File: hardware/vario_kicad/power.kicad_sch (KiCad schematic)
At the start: 25 parts, among them Q1 NMOS, Q2 PMOS, U4 USB C connector

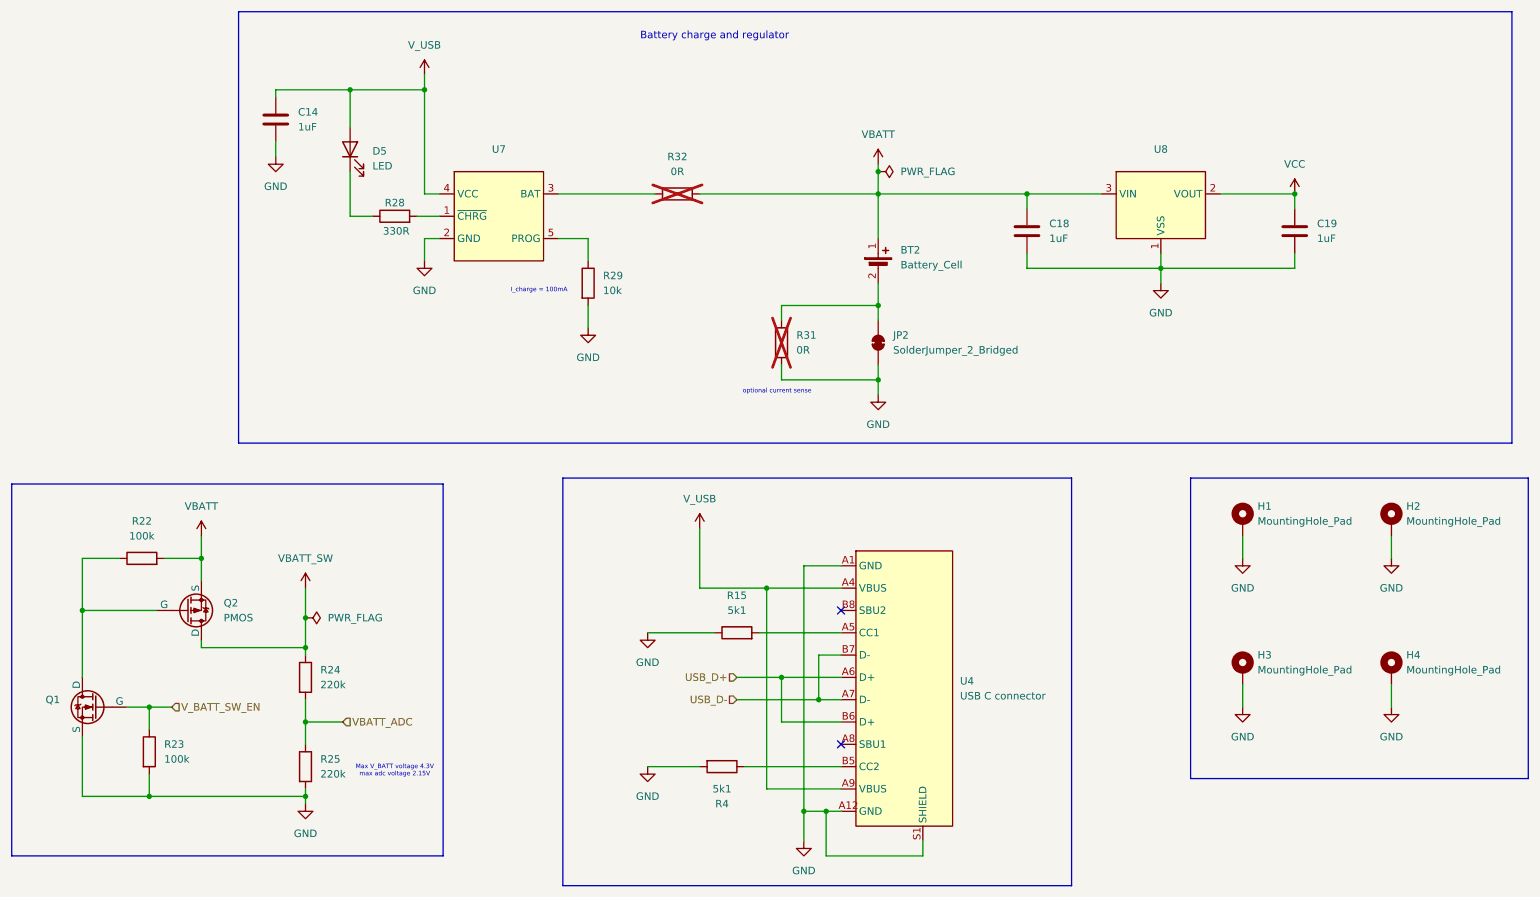
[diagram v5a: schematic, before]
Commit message: minor updates to power schematic
- add optional battery bypass resistor between USB power and 3.3V regulator
- make VBATT voltage divider use the more common 100k resistor
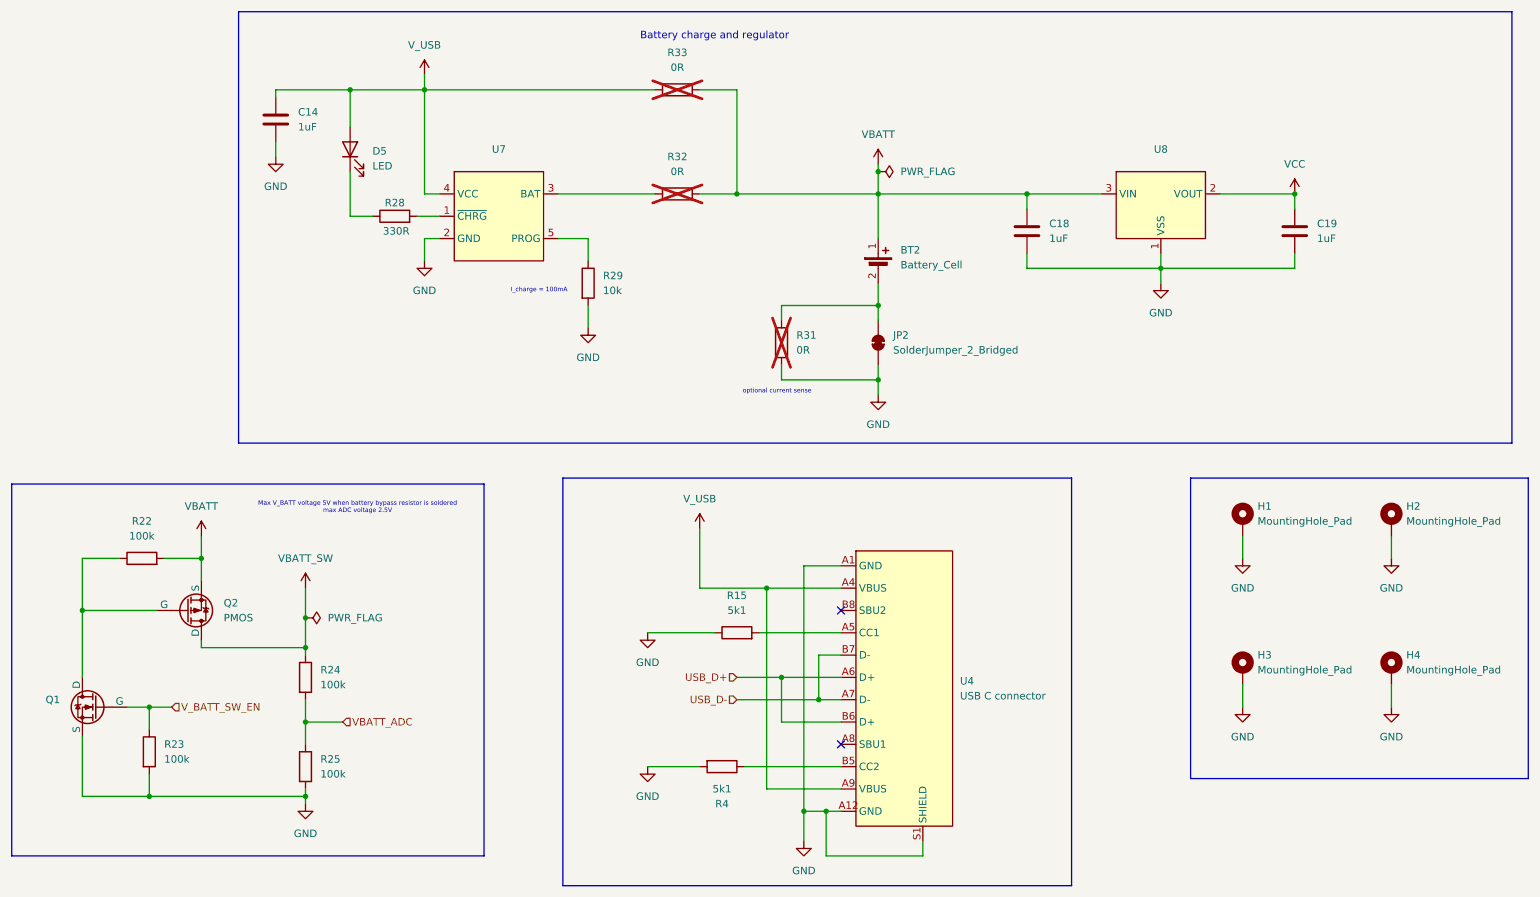
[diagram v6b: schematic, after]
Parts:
- added R33: 0R, Resistor_SMD:R_0402_1005Metric, symbol Device:R
- R24, R25: value 220k -> 100k
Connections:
- net VBATT: now also R33.2
- net V_USB: now also R33.1
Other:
- note added: "Max V_BATT voltage 5V when battery bypass resistor is soldered max ADC voltage 2.5V"
- note removed: "Max V_BATT voltage 4.3V max adc voltage 2.15V"
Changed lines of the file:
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@@
+	)
+	(junction
+		(at 142.24 46.99)
+		(diameter 0)
+		(color 0 0 0 0)
 	)
 	(junction
@@
 	(wire
 		(pts
+			(xy 142.24 29.21) (xy 142.24 46.99)
+		)
+		(stroke
+			(width 0)
+			(type default)
+		)
+	)
+	(wire
+		(pts
 			(xy 116.84 66.04) (xy 116.84 69.85)
 		)
@@
 	(wire
 		(pts
+			(xy 135.89 29.21) (xy 142.24 29.21)
+		)
+		(stroke
+			(width 0)
+			(type default)
+		)
+	)
+	(wire
+		(pts
 			(xy 68.58 137.16) (xy 74.93 137.16)
 		)
@@
 	(wire
 		(pts
+			(xy 142.24 46.99) (xy 166.37 46.99)
+		)
+		(stroke
+			(width 0)
+			(type default)
+		)
+	)
+	(wire
+		(pts
 			(xy 30.48 118.11) (xy 43.18 118.11)
 		)
@@
 	(wire
 		(pts
-			(xy 135.89 46.99) (xy 166.37 46.99)
+			(xy 135.89 46.99) (xy 142.24 46.99)
 		)
 		(stroke
@@
 		(pts
 			(xy 166.37 76.2) (xy 166.37 78.74)
+		)
+		(stroke
+			(width 0)
+			(type default)
+		)
+	)
+	(wire
+		(pts
+			(xy 88.9 29.21) (xy 128.27 29.21)
 		)
 		(stroke
@@
 	(rectangle
 		(start 18.415 96.52)
-		(end 92.075 160.02)
+		(end 99.06 160.02)
 		(stroke
 			(width 0)
@@
 		)
 	)
-	(text "Max V_BATT voltage 4.3V\nmax adc voltage 2.15V"
+	(text "Max V_BATT voltage 5V when battery bypass resistor is soldered\nmax ADC voltage 2.5V"
 		(exclude_from_sim no)
-		(at 83.82 145.542 0)
+		(at 77.47 100.584 0)
 		(effects
 			(font
@@
 			)
 		)
-		(property "Value" "220k"
+		(property "Value" "100k"
 			(at 71.12 130.8099 0)
 			(effects
@@
 				(path "/50389aff-b244-451e-8e3a-c5addd2215e1/9ff7b2dd-70fe-4259-884c-1f1f10c7ad3d"
 					(reference "R24")
+					(unit 1)
+				)
+			)
+		)
+	)
+	(symbol
+		(lib_id "Device:R")
+		(at 132.08 29.21 90)
+		(mirror x)
+		(unit 1)
+		(exclude_from_sim no)
+		(in_bom yes)
+		(on_board yes)
+		(dnp yes)
+		(property "Reference" "R33"
+			(at 132.08 22.86 90)
+			(effects
+				(font
+					(size 1.27 1.27)
+				)
+			)
+		)
+		(property "Value" "0R"
+			(at 132.08 25.4 90)
+			(effects
+				(font
+					(size 1.27 1.27)
+				)
+			)
+		)
+		(property "Footprint" "Resistor_SMD:R_0402_1005Metric"
+			(at 132.08 27.432 90)
+			(effects
+				(font
+					(size 1.27 1.27)
+				)
+				(hide yes)
+			)
+		)
+		(property "Datasheet" "~"
+			(at 132.08 29.21 0)
+			(effects
+				(font
+					(size 1.27 1.27)
+				)
+				(hide yes)
+			)
+		)
+		(property "Description" "Resistor"
+			(at 132.08 29.21 0)
+			(effects
+				(font
+					(size 1.27 1.27)
+				)
+				(hide yes)
+			)
+		)
+		(pin "2"
+		)
+		(pin "1"
+		)
+		(instances
+			(project ""
+				(path "/50389aff-b244-451e-8e3a-c5addd2215e1/9ff7b2dd-70fe-4259-884c-1f1f10c7ad3d"
+					(reference "R33")
 					(unit 1)
 				)
@@
 			)
 		)
-		(property "Value" "220k"
+		(property "Value" "100k"
 			(at 71.12 146.0499 0)
 			(effects
